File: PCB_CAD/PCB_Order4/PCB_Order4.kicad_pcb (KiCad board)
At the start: 4 copper layers, 116.2 x 115 mm, 82 parts

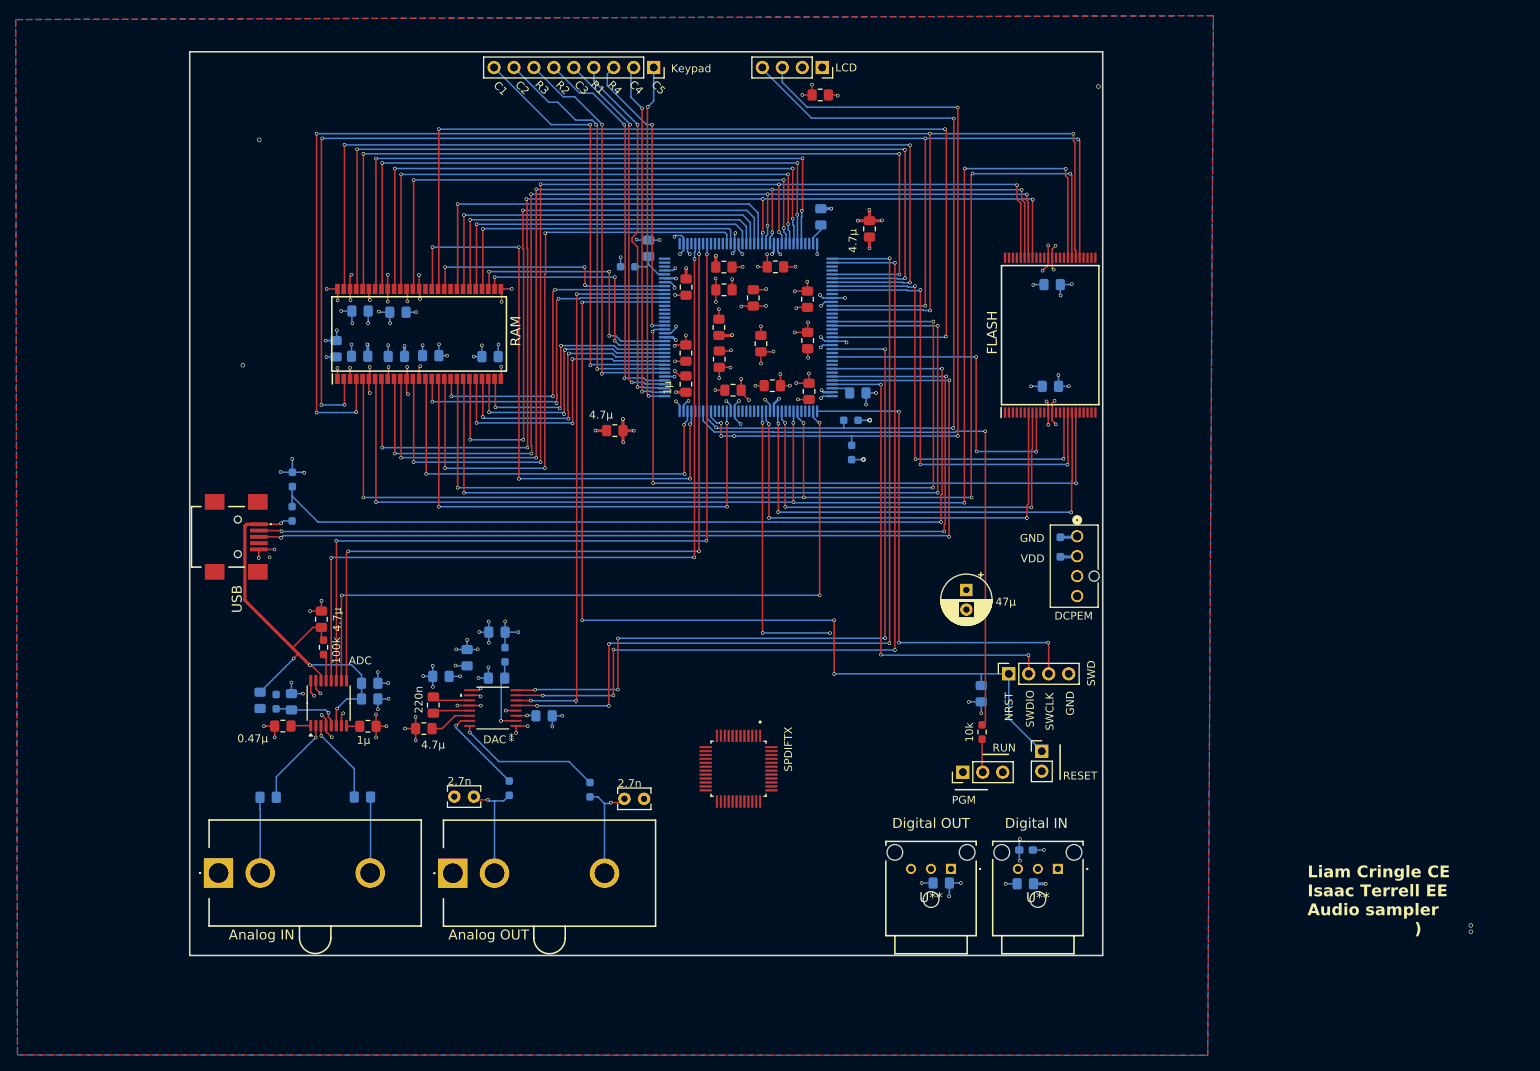
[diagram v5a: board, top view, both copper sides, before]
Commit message: substantive board revisions complete, needs one good review pass. CubeMX updated for I2S3 and DIR interrupt line
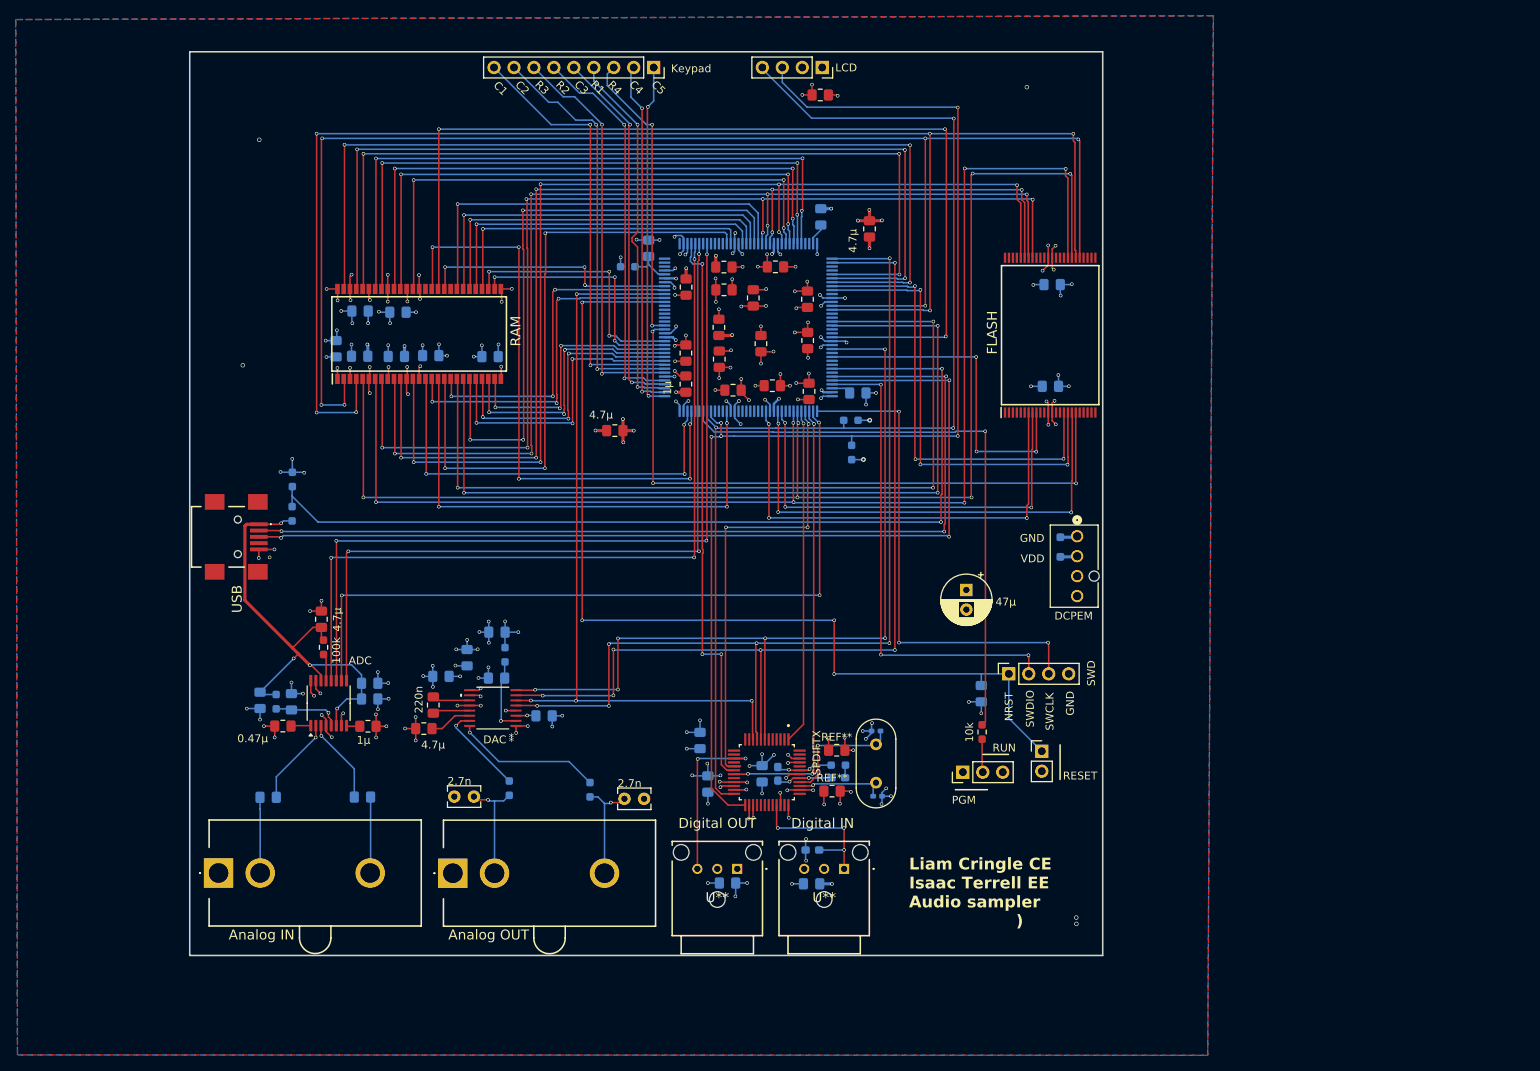
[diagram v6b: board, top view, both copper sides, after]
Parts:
- added REF**: C_0805_2012Metric_Pad1.18x1.45mm_HandSolder, Capacitor_SMD:C_0805_2012Metric_Pad1.18x1.45mm_HandSolder, F.Cu at (186.3, 118.3)
- added REF**: C_0603_1608Metric_Pad1.08x0.95mm_HandSolder, Capacitor_SMD:C_0603_1608Metric_Pad1.08x0.95mm_HandSolder, B.Cu at (179.4, 116.1)
- added REF**: C_0805_2012Metric_Pad1.18x1.45mm_HandSolder, Capacitor_SMD:C_0805_2012Metric_Pad1.18x1.45mm_HandSolder, B.Cu at (177.4, 116.1)
- added REF**: C_0603_1608Metric_Pad1.08x0.95mm_HandSolder, Capacitor_SMD:C_0603_1608Metric_Pad1.08x0.95mm_HandSolder, B.Cu at (187.1, 116.6)
- added REF**: C_0402_1005Metric_Pad0.74x0.62mm_HandSolder, Capacitor_SMD:C_0402_1005Metric_Pad0.74x0.62mm_HandSolder, B.Cu at (191.9, 110.7)
- added REF**: Crystal_HC49-U_Vertical, Crystal:Crystal_HC49-U_Vertical, F.Cu at (191.9, 112.3)
- added REF**: C_0805_2012Metric_Pad1.18x1.45mm_HandSolder, Capacitor_SMD:C_0805_2012Metric_Pad1.18x1.45mm_HandSolder, F.Cu at (186.9, 113.1)
- added REF**: C_0805_2012Metric_Pad1.18x1.45mm_HandSolder, Capacitor_SMD:C_0805_2012Metric_Pad1.18x1.45mm_HandSolder, B.Cu at (169.5, 111.9)
- added REF**: C_0805_2012Metric_Pad1.18x1.45mm_HandSolder, Capacitor_SMD:C_0805_2012Metric_Pad1.18x1.45mm_HandSolder, B.Cu at (170.5, 117.4)
- added REF**: R_0603_1608Metric_Pad0.98x0.95mm_HandSolder, Resistor_SMD:R_0603_1608Metric_Pad0.98x0.95mm_HandSolder, B.Cu at (187.1, 115.0)
- added REF**: C_0402_1005Metric_Pad0.74x0.62mm_HandSolder, Capacitor_SMD:C_0402_1005Metric_Pad0.74x0.62mm_HandSolder, B.Cu at (192.1, 119.0)
- moved REF** 27.2 mm to (183.7, 130.1)
- moved REF** 27.2 mm to (183.8, 125.8)
- moved REF** 27.2 mm to (173.0, 130.0)
- moved U** 27.2 mm to (187.8, 128.2)
- moved U** 27.2 mm to (174.2, 128.2)
- moved SPDIFTX 3.63 mm to (178.0, 115.9)
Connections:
- Microcontroller pad 111: SPDIF_ERR -> I2S3_BCK
- Microcontroller pad 112: unconnected-(uController1-PC11-Pad112) -> I2S3_DIN
- Microcontroller pad 113: unconnected-(uController1-PC12-Pad113) -> SPDIF_ERR
- Microcontroller pad 123: /SPDIFRX_IN0 -> unconnected-(uController1-PD7-Pad123)
- Microcontroller pad 40: unconnected-(uController1-PA4-Pad40) -> I2S3_LRCK
- SPDIFTX pad 17: unconnected-(SPDIFTX1-DOUT-Pad17) -> I2S3_DIN
- SPDIFTX pad 18: unconnected-(SPDIFTX1-LRCK-Pad18) -> I2S3_LRCK
- SPDIFTX pad 19: unconnected-(SPDIFTX1-BCK-Pad19) -> I2S3_BCK
- SPDIFTX pad 33: unconnected-(SPDIFTX1-RXIN2-Pad33) -> /SPDIFRX_IN0
- SPDIFTX pad 39: unconnected-(SPDIFTX1-XTI-Pad39) -> Crystal_XTI
- SPDIFTX pad 40: unconnected-(SPDIFTX1-XTO-Pad40) -> Crystal_XTO
- SPDIFTX pad 43: unconnected-(SPDIFTX1-FILT-Pad43) -> FILT
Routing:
- net I2S3_LRCK: track 0.00 -> 72.2 mm, vias 0 -> 3
- net I2S3_DIN: track 0.00 -> 58.4 mm, vias 0 -> 3
- net I2S3_BCK: track 0.00 -> 56.5 mm, vias 0 -> 3
- net GNDD: track 208.6 -> 260.2 mm, vias 144 -> 175
- net /I2C1_SCL: track 102.8 -> 153.9 mm
- net /I2C1_SDA: track 100.4 -> 148.9 mm
- net SPDIF_ERR: track 0.00 -> 42.7 mm, vias 0 -> 1
- net /I2S2_SDO: track 70.9 -> 98.0 mm, vias 3 -> 4
- net /SPDIFTX_OUT: track 0.00 -> 21.6 mm, vias 0 -> 2
- net /SPDIFRX_IN0: track 38.2 -> 19.8 mm, vias 4 -> 3
- net Crystal_XTO: track 0.00 -> 15.8 mm, vias 0 -> 1
- net VDD: track 99.9 -> 114.9 mm, vias 65 -> 74
- net /I2S2_MCK: track 97.1 -> 110.0 mm, vias 5 -> 6
- net /I2S2_WS: track 111.9 -> 124.2 mm, vias 5 -> 6
- net Crystal_XTI: track 0.00 -> 11.8 mm, vias 0 -> 1
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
